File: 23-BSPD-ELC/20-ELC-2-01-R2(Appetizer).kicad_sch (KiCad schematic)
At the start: 0 parts

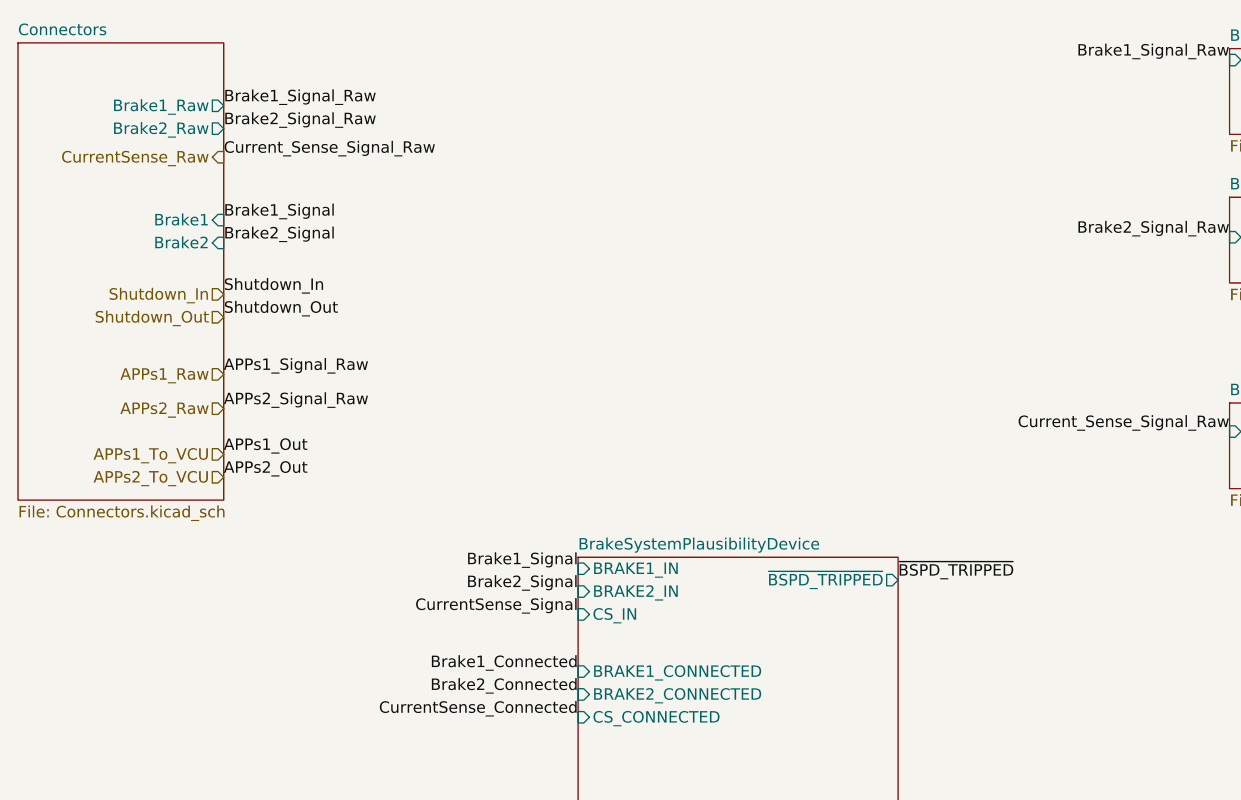
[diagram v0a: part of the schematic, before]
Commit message: Updated connectors and added ~brake signal to vcu
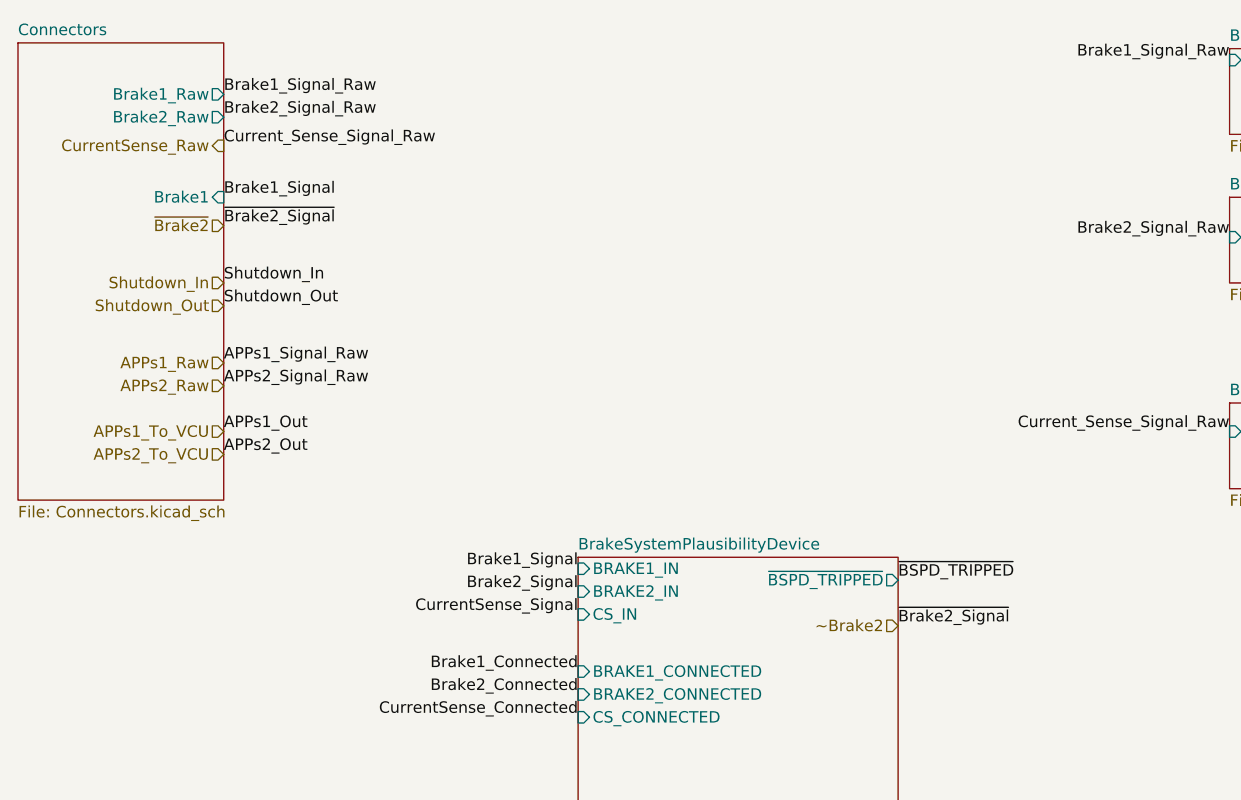
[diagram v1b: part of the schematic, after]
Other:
- sheet Connectors ports: added none; removed Brake2
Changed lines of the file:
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@@
     (effects (font (size 1.27 1.27)) (justify right bottom))
   )
-  (label "Current_Sense_Signal_Raw" (at 40.64 31.75 0)
+  (label "Current_Sense_Signal_Raw" (at 40.64 30.48 0)
     (effects (font (size 1.27 1.27)) (justify left bottom))
   )
@@
     (effects (font (size 1.27 1.27)) (justify right bottom))
   )
-  (label "Brake1_Signal_Raw" (at 40.64 26.035 0)
-    (effects (font (size 1.27 1.27)) (justify left bottom))
-  )
-  (label "Brake2_Signal_Raw" (at 40.64 28.575 0)
+  (label "~{Brake2_Signal}" (at 115.57 83.82 0)
+    (effects (font (size 1.27 1.27)) (justify left bottom))
+  )
+  (label "Brake1_Signal_Raw" (at 40.64 24.765 0)
+    (effects (font (size 1.27 1.27)) (justify left bottom))
+  )
+  (label "Brake2_Signal_Raw" (at 40.64 27.305 0)
+    (effects (font (size 1.27 1.27)) (justify left bottom))
+  )
+  (label "~{Brake2_Signal}" (at 40.64 39.37 0)
     (effects (font (size 1.27 1.27)) (justify left bottom))
   )
@@
     (effects (font (size 1.27 1.27)) (justify right bottom))
   )
-  (label "Shutdown_Out" (at 40.64 49.53 0)
+  (label "Shutdown_Out" (at 40.64 48.26 0)
     (effects (font (size 1.27 1.27)) (justify left bottom))
   )
@@
     (effects (font (size 1.27 1.27)) (justify left bottom))
   )
-  (label "APPs1_Out" (at 40.64 64.77 0)
+  (label "APPs1_Out" (at 40.64 62.23 0)
     (effects (font (size 1.27 1.27)) (justify left bottom))
   )
@@
     (effects (font (size 1.27 1.27)) (justify right bottom))
   )
-  (label "APPs2_Out" (at 40.64 67.31 0)
-    (effects (font (size 1.27 1.27)) (justify left bottom))
-  )
-  (label "Shutdown_In" (at 40.64 46.99 0)
+  (label "APPs2_Out" (at 40.64 64.77 0)
+    (effects (font (size 1.27 1.27)) (justify left bottom))
+  )
+  (label "Shutdown_In" (at 40.64 45.72 0)
     (effects (font (size 1.27 1.27)) (justify left bottom))
   )
@@
     (effects (font (size 1.27 1.27)) (justify right bottom))
   )
-  (label "APPs2_Signal_Raw" (at 40.64 59.69 0)
+  (label "APPs2_Signal_Raw" (at 40.64 57.15 0)
     (effects (font (size 1.27 1.27)) (justify left bottom))
   )
@@
     (effects (font (size 1.27 1.27)) (justify right bottom))
   )
-  (label "Brake1_Signal" (at 40.64 38.735 0)
+  (label "Brake1_Signal" (at 40.64 36.195 0)
     (effects (font (size 1.27 1.27)) (justify left bottom))
   )
@@
     (effects (font (size 1.27 1.27)) (justify right bottom))
   )
-  (label "APPs1_Signal_Raw" (at 40.64 55.88 0)
+  (label "APPs1_Signal_Raw" (at 40.64 54.61 0)
     (effects (font (size 1.27 1.27)) (justify left bottom))
   )
@@
     (effects (font (size 1.27 1.27)) (justify left bottom))
   )
-  (label "Brake2_Signal" (at 40.64 41.275 0)
-    (effects (font (size 1.27 1.27)) (justify left bottom))
-  )
   (label "APPs2_25%" (at 142.24 128.27 180)
     (effects (font (size 1.27 1.27)) (justify right bottom))
@@
     (effects (font (size 1.27 1.27)) (justify right))
   )
-  (hierarchical_label "APPs1_Raw" (shape input) (at 40.64 55.88 180)
+  (hierarchical_label "APPs1_Raw" (shape input) (at 40.64 54.61 180)
     (effects (font (size 1.27 1.27)) (justify right))
   )
@@
     (effects (font (size 1.27 1.27)) (justify left))
   )
+  (hierarchical_label "~Brake2" (shape input) (at 115.57 83.82 180)
+    (effects (font (size 1.27 1.27)) (justify right))
+  )
   (hierarchical_label "Shutdown_IN" (shape input) (at 55.88 153.67 0)
     (effects (font (size 1.27 1.27)) (justify left))
   )
-  (hierarchical_label "APPs2_To_VCU" (shape input) (at 40.64 67.31 180)
+  (hierarchical_label "APPs2_To_VCU" (shape input) (at 40.64 64.77 180)
     (effects (font (size 1.27 1.27)) (justify right))
   )
@@
     (effects (font (size 1.27 1.27)) (justify right))
   )
-  (hierarchical_label "Shutdown_Out" (shape input) (at 40.64 49.53 180)
+  (hierarchical_label "Shutdown_Out" (shape input) (at 40.64 48.26 180)
     (effects (font (size 1.27 1.27)) (justify right))
   )
@@
     (effects (font (size 1.27 1.27)) (justify right))
   )
-  (hierarchical_label "APPs1_To_VCU" (shape input) (at 40.64 64.77 180)
+  (hierarchical_label "APPs1_To_VCU" (shape input) (at 40.64 62.23 180)
     (effects (font (size 1.27 1.27)) (justify right))
   )
@@
     (effects (font (size 1.27 1.27)) (justify left))
   )
+  (hierarchical_label "~{Brake2}" (shape input) (at 40.64 39.37 180)
+    (effects (font (size 1.27 1.27)) (justify right))
+  )
   (hierarchical_label "APPs2_Signal" (shape input) (at 142.24 151.13 0)
     (effects (font (size 1.27 1.27)) (justify left))
@@
     (effects (font (size 1.27 1.27)) (justify left))
   )
-  (hierarchical_label "Shutdown_In" (shape input) (at 40.64 46.99 180)
+  (hierarchical_label "Shutdown_In" (shape input) (at 40.64 45.72 180)
     (effects (font (size 1.27 1.27)) (justify right))
   )
@@
     (effects (font (size 1.27 1.27)) (justify left))
   )
-  (hierarchical_label "CurrentSense_Raw" (shape output) (at 40.64 31.75 180)
+  (hierarchical_label "CurrentSense_Raw" (shape output) (at 40.64 30.48 180)
     (effects (font (size 1.27 1.27)) (justify right))
   )
@@
     (effects (font (size 1.27 1.27)) (justify right))
   )
-  (hierarchical_label "APPs2_Raw" (shape input) (at 40.64 59.69 180)
+  (hierarchical_label "APPs2_Raw" (shape input) (at 40.64 57.15 180)
     (effects (font (size 1.27 1.27)) (justify right))
   )
@@
       (effects (font (size 1.27 1.27)) (justify left top))
     )
-    (pin "Brake1_Raw" output (at 40.64 26.035 0)
+    (pin "Brake1_Raw" output (at 40.64 24.765 0)
       (effects (font (size 1.27 1.27)) (justify right))
     )
-    (pin "Brake2_Raw" output (at 40.64 28.575 0)
+    (pin "Brake2_Raw" output (at 40.64 27.305 0)
       (effects (font (size 1.27 1.27)) (justify right))
     )
-    (pin "Brake1" input (at 40.64 38.735 0)
-      (effects (font (size 1.27 1.27)) (justify right))
-    )
-    (pin "Brake2" input (at 40.64 41.275 0)
+    (pin "Brake1" input (at 40.64 36.195 0)
       (effects (font (size 1.27 1.27)) (justify right))
     )
@@
       (reference "#PWR04") (unit 1) (value "GND") (footprint "")
     )
-    (path "/00000000-0000-0000-0000-00005d9a6d3a/00000000-0000-0000-0000-00006240da50"
-      (reference "#PWR05") (unit 1) (value "GND") (footprint "")
-    )
     (path "/00000000-0000-0000-0000-00005d9a6d3a/00000000-0000-0000-0000-000061bc8d7f"
       (reference "#PWR06") (unit 1) (value "GND") (footprint "")
@@
       (reference "H4") (unit 1) (value "MountingHole") (footprint "MountingHole:MountingHole_3.7mm_Pad_TopBottom")
     )
-    (path "/00000000-0000-0000-0000-00005d922b3a/92deafad-57c4-45f5-b724-ada2e8983703"
-      (reference "J1") (unit 1) (value "Conn_02x06_Counter_Clockwise") (footprint "")
-    )
     (path "/d56944af-8ec3-4bc9-b6e5-f0f211b6d661/b26b28b6-360d-4e7e-b9d2-d9b3f9bcd50f/27fec5df-f50a-420e-8f18-082a387b0bca"
       (reference "J2") (unit 1) (value "Conn_01x02") (footprint "Connector_PinHeader_2.54mm:PinHeader_1x02_P2.54mm_Vertical")
@@
       (reference "J4") (unit 1) (value "SWD") (footprint "Connector_PinHeader_1.27mm:PinHeader_2x03_P1.27mm_Vertical")
     )
+    (path "/00000000-0000-0000-0000-00005d922b3a/39cc31f3-257f-47f1-a11e-739077dcf1c6"
+      (reference "J?") (unit 1) (value "Conn_02x08_Counter_Clockwise") (footprint "")
+    )
     (path "/d56944af-8ec3-4bc9-b6e5-f0f211b6d661/b26b28b6-360d-4e7e-b9d2-d9b3f9bcd50f/af358307-4e47-4011-a445-f75ae1a48b0c"

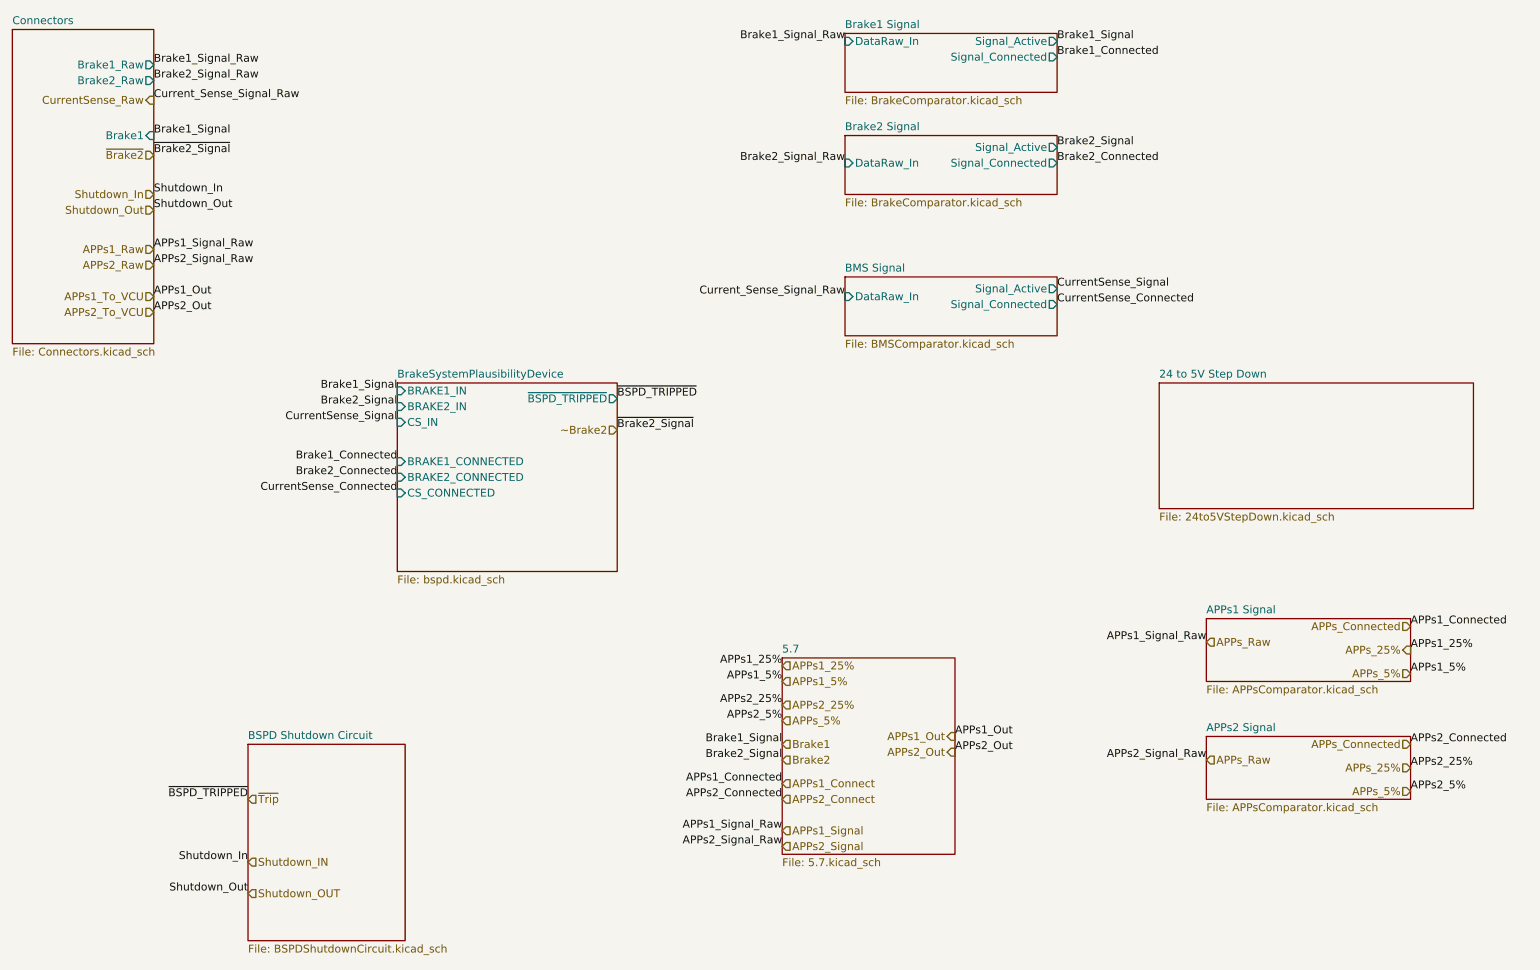
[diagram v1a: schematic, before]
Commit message: Revision changes and updates to some footprints
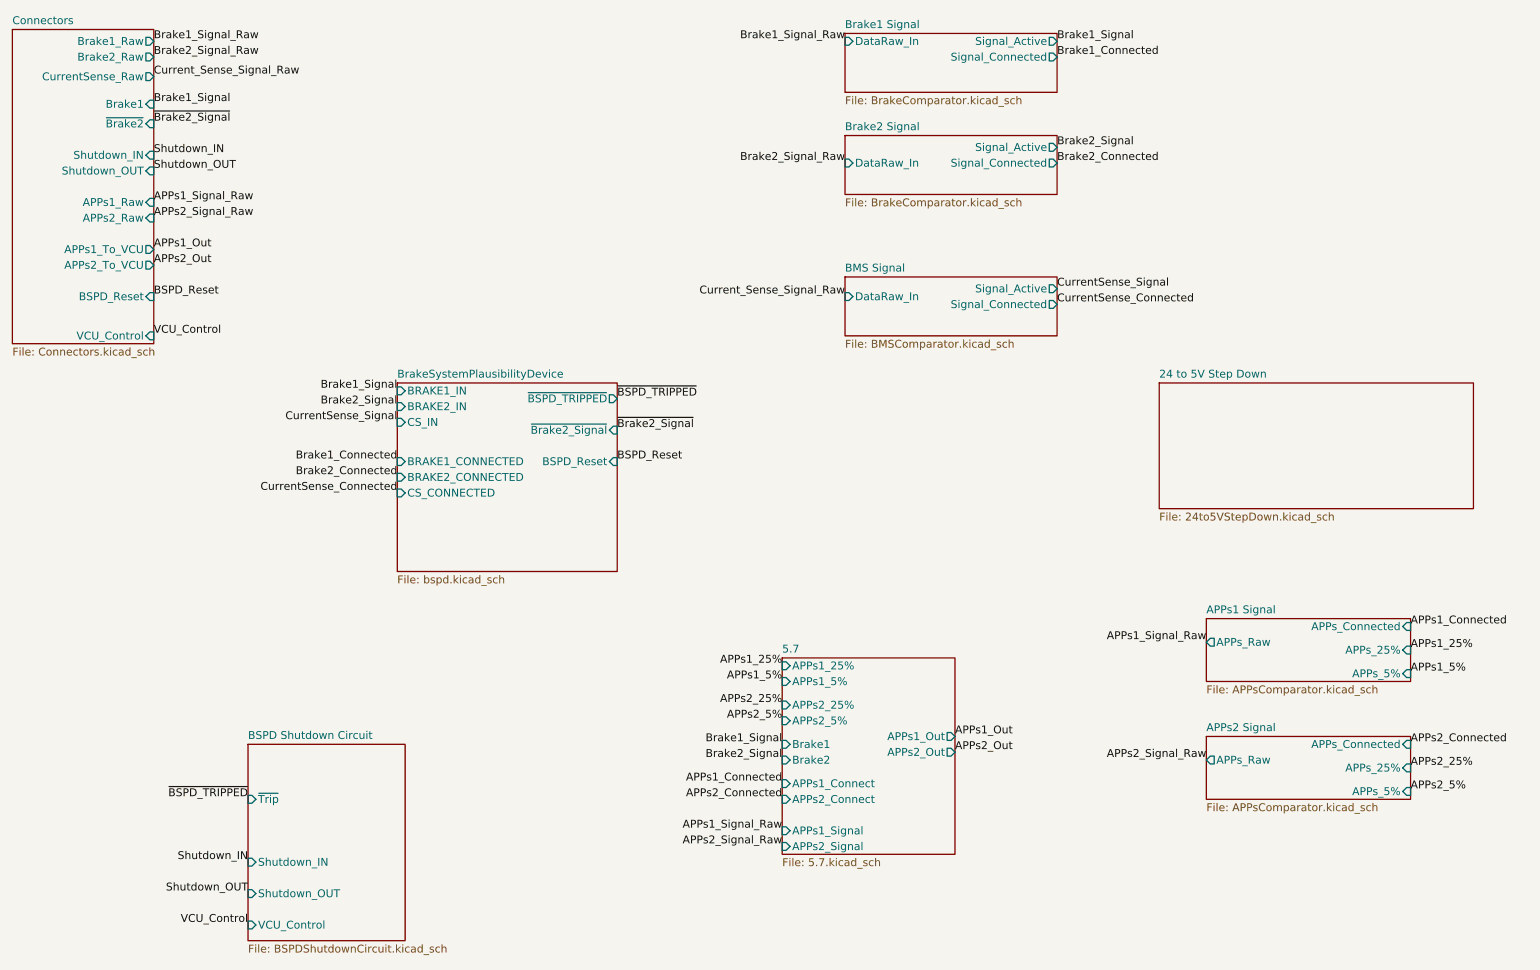
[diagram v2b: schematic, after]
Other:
- sheet 5.7 ports: added APPs1_25%, APPs1_5%, APPs1_Connect, APPs1_Out, APPs1_Signal, APPs2_25%, APPs2_5%, APPs2_Connect, APPs2_Out, APPs2_Signal, Brake1, Brake2; removed none
- sheet APPs1 Signal ports: added APPs_25%, APPs_5%, APPs_Connected, APPs_Raw; removed none
- sheet APPs2 Signal ports: added APPs_25%, APPs_5%, APPs_Connected, APPs_Raw; removed none
- sheet BSPD Shutdown Circuit ports: added Shutdown_IN, Shutdown_OUT, VCU_Control, ~{Trip}; removed none
- sheet BrakeSystemPlausibilityDevice ports: added BSPD_Reset, ~{Brake2_Signal}; removed none
- sheet Connectors ports: added APPs1_Raw, APPs1_To_VCU, APPs2_Raw, APPs2_To_VCU, BSPD_Reset, CurrentSense_Raw, Shutdown_IN, Shutdown_OUT, VCU_Control, ~{Brake2}; removed none

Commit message: BSPD layout
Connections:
- no-connect marks 0 -> 4
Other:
- added sheet Watchdog (Watchdog.kicad_sch)
